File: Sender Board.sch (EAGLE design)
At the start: 11 parts, among them IC2 PIC16F1826/27SO, J1 PIC_ICSP_MINI_5_PIN, U1 915MHz, X1 87758-0216, X2 BU-SMA-V

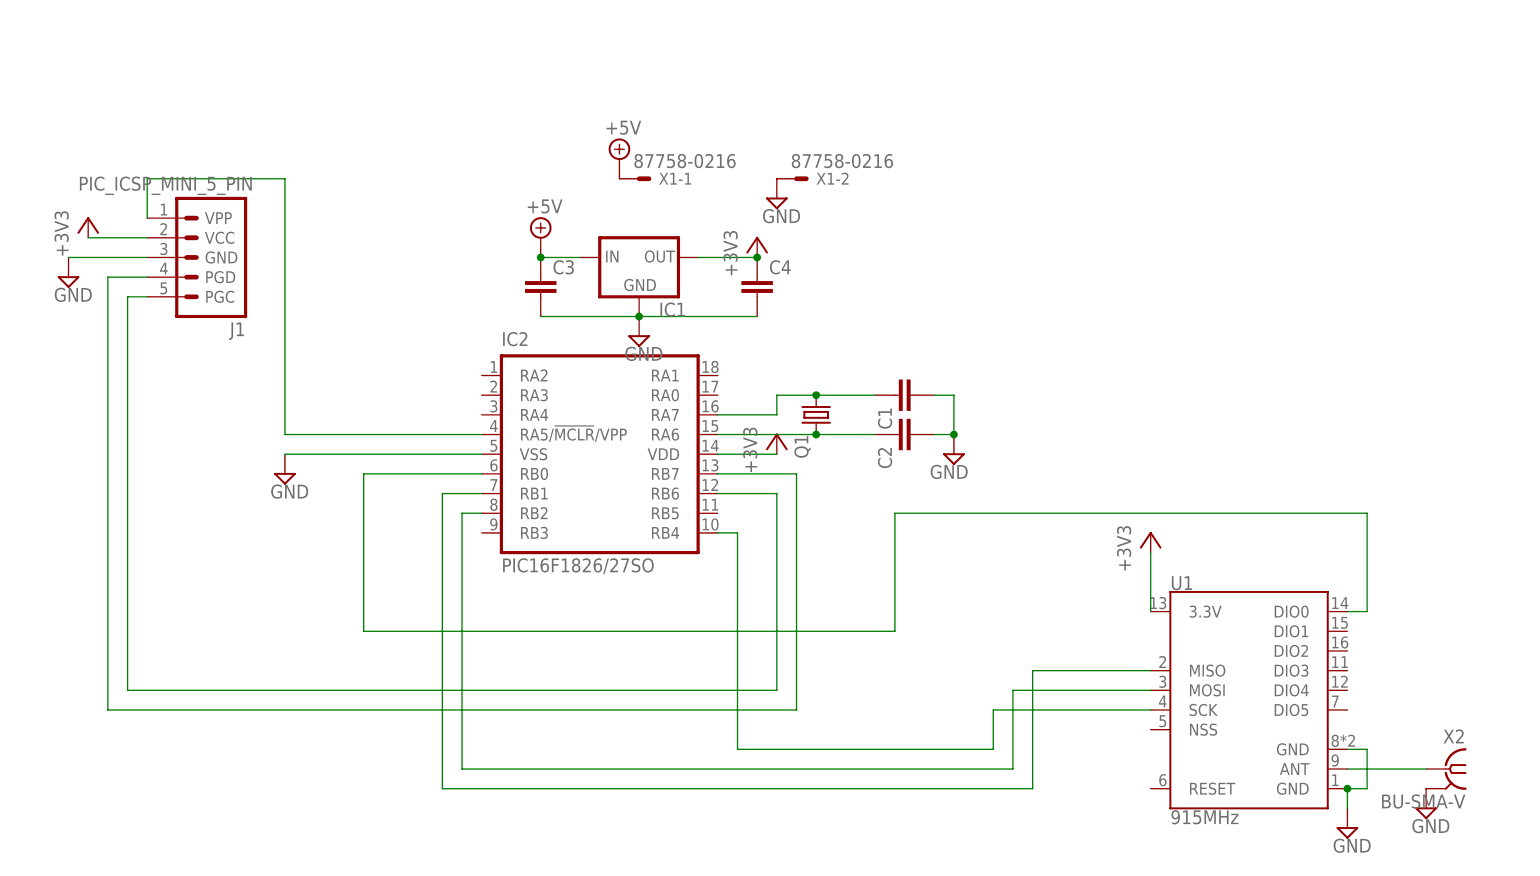
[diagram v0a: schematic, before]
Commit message: Ordered sender PCB
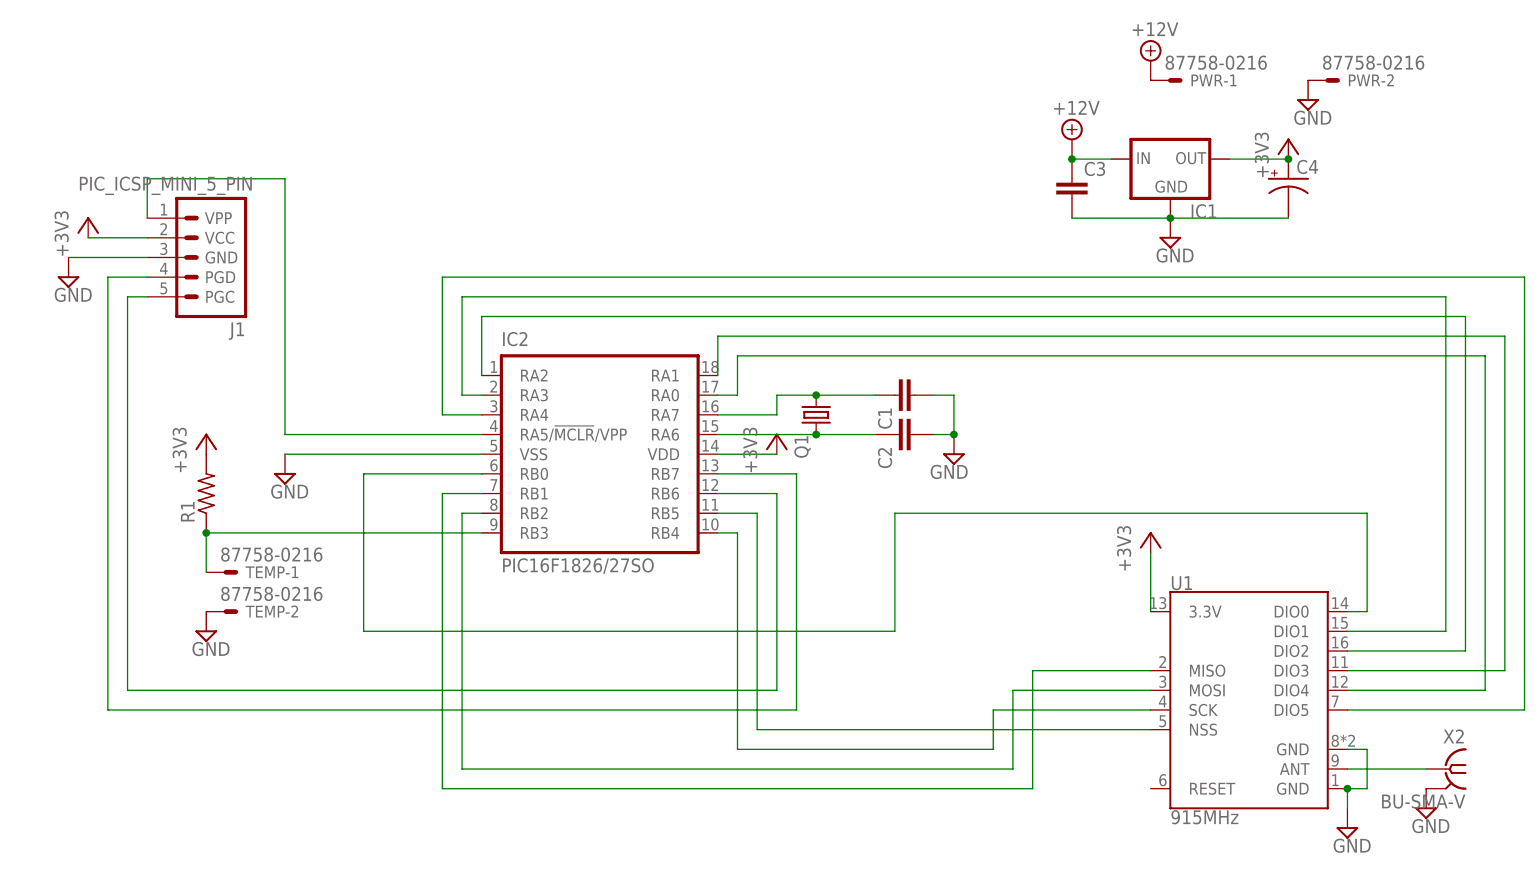
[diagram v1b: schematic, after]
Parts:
- removed X1: 87758-0216, con-molex:87758-0216
- added PWR, TEMP: 87758-0216, con-molex:87758-0216
- added R1: (no value), resistor:R-US_0204/7
- C4: device resistor:C-EU050-025X075 -> resistor:CPOL-USE3.5-8
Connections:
- net N$4 renamed MISO
- net N$5 renamed MOSI
- net N$6 renamed SCK
- removed net +5V: C3.1, IC1.IN, X1-1.S
- new net +12V: C3.1, IC1.IN, PWR-1.S
- new net N$11: IC2.RB3, R1.1, TEMP-1.S
- new net N$12: IC2.RB5, U1.NSS
- new net N$13: IC2.RA1, U1.DIO3
- new net N$14: IC2.RA0, U1.DIO4
- new net N$15: IC2.RA2, U1.DIO2
- new net N$16: IC2.RA3, U1.DIO1
- new net N$17: IC2.RA4, U1.DIO5
- net +3V3: now also C4.+, R1.2; no longer C4.1
- net GND: now also C4.-, PWR-2.S, TEMP-2.S; no longer C4.2, X1-2.S
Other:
- moved on the sheet: C3, IC1
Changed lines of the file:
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@@
 <parts>
 <part name="U1" library="SparkFun-RF" deviceset="RFM69H" device="CW-915" value="915MHz"/>
-<part name="X1" library="con-molex" deviceset="87758-0216" device=""/>
-<part name="SUPPLY1" library="supply2" deviceset="+5V" device=""/>
+<part name="PWR" library="con-molex" deviceset="87758-0216" device=""/>
 <part name="SUPPLY2" library="supply2" deviceset="GND" device=""/>
 <part name="SUPPLY3" library="supply2" deviceset="GND" device=""/>
 <part name="IC1" library="v-reg" deviceset="78LXX" device=""/>
 <part name="SUPPLY4" library="supply2" deviceset="GND" device=""/>
-<part name="SUPPLY5" library="supply2" deviceset="+5V" device=""/>
 <part name="+3V1" library="supply1" deviceset="+3V3" device=""/>
 <part name="+3V2" library="supply1" deviceset="+3V3" device=""/>
@@
 <part name="SUPPLY9" library="supply2" deviceset="GND" device=""/>
 <part name="C3" library="resistor" deviceset="C-EU" device="050-025X075"/>
-<part name="C4" library="resistor" deviceset="C-EU" device="050-025X075"/>
+<part name="C4" library="resistor" deviceset="CPOL-US" device="E3.5-8"/>
+<part name="R1" library="resistor" deviceset="R-US_" device="0204/7"/>
+<part name="TEMP" library="con-molex" deviceset="87758-0216" device=""/>
+<part name="SUPPLY10" library="supply2" deviceset="GND" device=""/>
+<part name="+3V5" library="supply1" deviceset="+3V3" device=""/>
+<part name="SUPPLY1" library="supply2" deviceset="+12V" device=""/>
+<part name="SUPPLY5" library="supply2" deviceset="+12V" device=""/>
 </parts>
 <sheets>
@@
 <instances>
 <instance part="U1" gate="G$1" x="88.9" y="25.4"/>
-<instance part="X1" gate="-1" x="10.16" y="93.98"/>
-<instance part="X1" gate="-2" x="30.48" y="93.98"/>
-<instance part="SUPPLY1" gate="+5V" x="7.62" y="96.52"/>
-<instance part="SUPPLY2" gate="GND" x="27.94" y="91.44"/>
+<instance part="PWR" gate="-1" x="78.74" y="106.68"/>
+<instance part="PWR" gate="-2" x="99.06" y="106.68"/>
+<instance part="SUPPLY2" gate="GND" x="96.52" y="104.14"/>
 <instance part="SUPPLY3" gate="GND" x="101.6" y="10.16"/>
-<instance part="IC1" gate="1" x="10.16" y="83.82"/>
-<instance part="SUPPLY4" gate="GND" x="10.16" y="73.66"/>
-<instance part="SUPPLY5" gate="+5V" x="-2.54" y="86.36"/>
-<instance part="+3V1" gate="G$1" x="25.4" y="86.36"/>
+<instance part="IC1" gate="1" x="78.74" y="96.52"/>
+<instance part="SUPPLY4" gate="GND" x="78.74" y="86.36"/>
+<instance part="+3V1" gate="G$1" x="93.98" y="99.06"/>
 <instance part="+3V2" gate="G$1" x="76.2" y="48.26"/>
 <instance part="+3V3" gate="G$1" x="27.94" y="60.96"/>
@@
 <instance part="X2" gate="G$1" x="114.3" y="17.78" rot="MR0"/>
 <instance part="SUPPLY9" gate="GND" x="111.76" y="12.7"/>
-<instance part="C3" gate="G$1" x="-2.54" y="81.28"/>
-<instance part="C4" gate="G$1" x="25.4" y="81.28"/>
+<instance part="C3" gate="G$1" x="66.04" y="93.98"/>
+<instance part="C4" gate="G$1" x="93.98" y="93.98"/>
+<instance part="R1" gate="G$1" x="-45.72" y="53.34" rot="R90"/>
+<instance part="TEMP" gate="-1" x="-43.18" y="43.18"/>
+<instance part="TEMP" gate="-2" x="-43.18" y="38.1"/>
+<instance part="SUPPLY10" gate="GND" x="-45.72" y="35.56"/>
+<instance part="+3V5" gate="G$1" x="-45.72" y="60.96"/>
+<instance part="SUPPLY1" gate="+12V" x="76.2" y="109.22"/>
+<instance part="SUPPLY5" gate="+12V" x="66.04" y="99.06"/>
 </instances>
 <busses>
 </busses>
 <nets>
-<net name="+5V" class="0">
-<segment>
-<pinref part="X1" gate="-1" pin="S"/>
-<pinref part="SUPPLY1" gate="+5V" pin="+5V"/>
-</segment>
-<segment>
-<pinref part="IC1" gate="1" pin="IN"/>
-<pinref part="SUPPLY5" gate="+5V" pin="+5V"/>
-<wire x1="-2.54" y1="83.82" x2="2.54" y2="83.82" width="0.1524" layer="91"/>
-<pinref part="C3" gate="G$1" pin="1"/>
-<junction x="-2.54" y="83.82"/>
-</segment>
-</net>
 <net name="GND" class="0">
 <segment>
-<pinref part="X1" gate="-2" pin="S"/>
+<pinref part="PWR" gate="-2" pin="S"/>
 <pinref part="SUPPLY2" gate="GND" pin="GND"/>
 </segment>
@@
 <pinref part="SUPPLY4" gate="GND" pin="GND"/>
 <pinref part="C3" gate="G$1" pin="2"/>
-<wire x1="-2.54" y1="76.2" x2="10.16" y2="76.2" width="0.1524" layer="91"/>
-<junction x="10.16" y="76.2"/>
-<pinref part="C4" gate="G$1" pin="2"/>
-<wire x1="25.4" y1="76.2" x2="10.16" y2="76.2" width="0.1524" layer="91"/>
+<wire x1="66.04" y1="88.9" x2="78.74" y2="88.9" width="0.1524" layer="91"/>
+<junction x="78.74" y="88.9"/>
+<pinref part="C4" gate="G$1" pin="-"/>
+<wire x1="93.98" y1="88.9" x2="78.74" y2="88.9" width="0.1524" layer="91"/>
 </segment>
 <segment>
@@
 <pinref part="SUPPLY9" gate="GND" pin="GND"/>
 </segment>
+<segment>
+<pinref part="TEMP" gate="-2" pin="S"/>
+<pinref part="SUPPLY10" gate="GND" pin="GND"/>
+</segment>
 </net>
 <net name="+3V3" class="0">
@@
 <pinref part="IC1" gate="1" pin="OUT"/>
 <pinref part="+3V1" gate="G$1" pin="+3V3"/>
-<wire x1="25.4" y1="83.82" x2="17.78" y2="83.82" width="0.1524" layer="91"/>
-<pinref part="C4" gate="G$1" pin="1"/>
-<junction x="25.4" y="83.82"/>
+<wire x1="93.98" y1="96.52" x2="86.36" y2="96.52" width="0.1524" layer="91"/>
+<pinref part="C4" gate="G$1" pin="+"/>
+<junction x="93.98" y="96.52"/>
 </segment>
 <segment>
@@
 <pinref part="+3V3" gate="G$1" pin="+3V3"/>
 <wire x1="27.94" y1="58.42" x2="20.32" y2="58.42" width="0.1524" layer="91"/>
+</segment>
+<segment>
+<pinref part="R1" gate="G$1" pin="2"/>
+<pinref part="+3V5" gate="G$1" pin="+3V3"/>
 </segment>
 </net>
@@
 </segment>
 </net>
-<net name="N$4" class="0">
+<net name="MISO" class="0">
 <segment>
 <pinref part="IC2" gate="G$1" pin="RB1"/>
@@
 </segment>
 </net>
-<net name="N$5" class="0">
+<net name="MOSI" class="0">
 <segment>
 <pinref part="IC2" gate="G$1" pin="RB2"/>
@@
 </segment>
 </net>
-<net name="N$6" class="0">
+<net name="SCK" class="0">
 <segment>
 <pinref part="IC2" gate="G$1" pin="RB4"/>
@@
 </segment>
 </net>
+<net name="N$11" class="0">
+<segment>
+<pinref part="R1" gate="G$1" pin="1"/>
+<pinref part="TEMP" gate="-1" pin="S"/>
+<wire x1="-45.72" y1="48.26" x2="-45.72" y2="43.18" width="0.1524" layer="91"/>
+<pinref part="IC2" gate="G$1" pin="RB3"/>
+<wire x1="-10.16" y1="48.26" x2="-45.72" y2="48.26" width="0.1524" layer="91"/>
+<junction x="-45.72" y="48.26"/>
+</segment>
+</net>
+<net name="N$12" class="0">
+<segment>
+<pinref part="IC2" gate="G$1" pin="RB5"/>
+<wire x1="20.32" y1="50.8" x2="25.4" y2="50.8" width="0.1524" layer="91"/>
+<wire x1="25.4" y1="50.8" x2="25.4" y2="22.86" width="0.1524" layer="91"/>
+<pinref part="U1" gate="G$1" pin="NSS"/>
+<wire x1="25.4" y1="22.86" x2="76.2" y2="22.86" width="0.1524" layer="91"/>
+</segment>
+</net>
+<net name="N$13" class="0">
+<segment>
+<pinref part="U1" gate="G$1" pin="DIO3"/>
+<wire x1="101.6" y1="30.48" x2="121.92" y2="30.48" width="0.1524" layer="91"/>
+<wire x1="121.92" y1="30.48" x2="121.92" y2="73.66" width="0.1524" layer="91"/>
+<pinref part="IC2" gate="G$1" pin="RA1"/>
+<wire x1="121.92" y1="73.66" x2="20.32" y2="73.66" width="0.1524" layer="91"/>
+<wire x1="20.32" y1="73.66" x2="20.32" y2="68.58" width="0.1524" layer="91"/>
+</segment>
+</net>
+<net name="N$14" class="0">
+<segment>
+<pinref part="IC2" gate="G$1" pin="RA0"/>
+<wire x1="20.32" y1="66.04" x2="22.86" y2="66.04" width="0.1524" layer="91"/>
+<wire x1="22.86" y1="66.04" x2="22.86" y2="71.12" width="0.1524" layer="91"/>
+<wire x1="22.86" y1="71.12" x2="119.38" y2="71.12" width="0.1524" layer="91"/>
+<wire x1="119.38" y1="71.12" x2="119.38" y2="27.94" width="0.1524" layer="91"/>
+<pinref part="U1" gate="G$1" pin="DIO4"/>
+<wire x1="119.38" y1="27.94" x2="101.6" y2="27.94" width="0.1524" layer="91"/>
+</segment>
+</net>
+<net name="N$15" class="0">
+<segment>
+<pinref part="U1" gate="G$1" pin="DIO2"/>
+<wire x1="101.6" y1="33.02" x2="116.84" y2="33.02" width="0.1524" layer="91"/>
+<wire x1="116.84" y1="33.02" x2="116.84" y2="76.2" width="0.1524" layer="91"/>
+<pinref part="IC2" gate="G$1" pin="RA2"/>
+<wire x1="116.84" y1="76.2" x2="-10.16" y2="76.2" width="0.1524" layer="91"/>
+<wire x1="-10.16" y1="76.2" x2="-10.16" y2="68.58" width="0.1524" layer="91"/>
+</segment>
+</net>
+<net name="N$16" class="0">
+<segment>
+<pinref part="U1" gate="G$1" pin="DIO1"/>
+<wire x1="101.6" y1="35.56" x2="114.3" y2="35.56" width="0.1524" layer="91"/>
+<wire x1="114.3" y1="35.56" x2="114.3" y2="78.74" width="0.1524" layer="91"/>
+<wire x1="114.3" y1="78.74" x2="-12.7" y2="78.74" width="0.1524" layer="91"/>
+<wire x1="-12.7" y1="78.74" x2="-12.7" y2="66.04" width="0.1524" layer="91"/>
+<pinref part="IC2" gate="G$1" pin="RA3"/>
+<wire x1="-12.7" y1="66.04" x2="-10.16" y2="66.04" width="0.1524" layer="91"/>
+</segment>
+</net>
+<net name="N$17" class="0">
+<segment>
+<pinref part="U1" gate="G$1" pin="DIO5"/>
+<wire x1="101.6" y1="25.4" x2="124.46" y2="25.4" width="0.1524" layer="91"/>
+<wire x1="124.46" y1="25.4" x2="124.46" y2="81.28" width="0.1524" layer="91"/>
+<wire x1="124.46" y1="81.28" x2="-15.24" y2="81.28" width="0.1524" layer="91"/>
+<wire x1="-15.24" y1="81.28" x2="-15.24" y2="63.5" width="0.1524" layer="91"/>
+<pinref part="IC2" gate="G$1" pin="RA4"/>
+<wire x1="-15.24" y1="63.5" x2="-10.16" y2="63.5" width="0.1524" layer="91"/>
+</segment>
+</net>
+<net name="+12V" class="0">
+<segment>
+<pinref part="PWR" gate="-1" pin="S"/>
+<pinref part="SUPPLY1" gate="+12V" pin="+12V"/>
+</segment>
+<segment>
+<pinref part="IC1" gate="1" pin="IN"/>
+<wire x1="66.04" y1="96.52" x2="71.12" y2="96.52" width="0.1524" layer="91"/>
+<pinref part="C3" gate="G$1" pin="1"/>
+<pinref part="SUPPLY5" gate="+12V" pin="+12V"/>
+<junction x="66.04" y="96.52"/>
+</segment>
+</net>
